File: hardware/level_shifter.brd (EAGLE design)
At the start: 15.2 x 12.7 mm, 14 parts, among them Q1 BS170, Q2 BS170

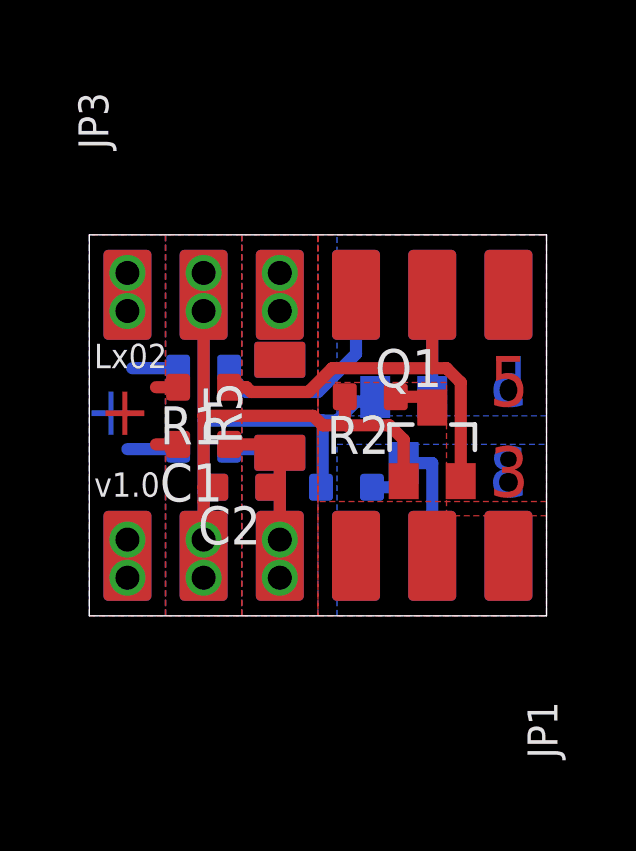
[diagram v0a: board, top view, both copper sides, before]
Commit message: shrunk level_shifter by one signal pinhead
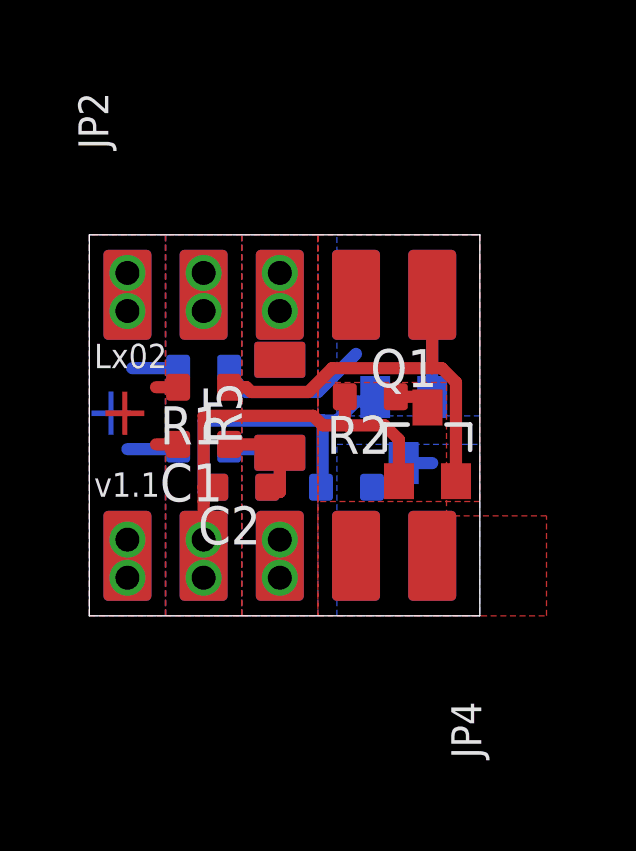
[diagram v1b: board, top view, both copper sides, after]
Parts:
- removed JP1, JP3: PINH2X06, pinhead_smd:PINH2X06SMD
- added JP2, JP4: PINH2X05, pinhead_smd:PINH2X05SMD
- moved Q1 0.16 mm to (11.3, 5.71)
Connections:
- net +3V3: now also JP2.B2, JP2.T2, JP4.B4, JP4.T4; no longer JP1.B5, JP1.T5, JP3.B2, JP3.T2
- net +5V: now also JP2.B1, JP2.T1, JP4.B5, JP4.T5; no longer JP1.B6, JP1.T6, JP3.B1, JP3.T1
- net GND: now also JP2.B3, JP2.T3, JP4.B3, JP4.T3; no longer JP1.B4, JP1.T4, JP3.B3, JP3.T3
- net IN_B: now also JP4.B1, JP4.B2; no longer JP1.B1, JP1.B2, JP1.B3
- net IN_T: now also JP4.T1, JP4.T2; no longer JP1.T1, JP1.T2, JP1.T3
- net OUT_B: now also JP2.B4, JP2.B5; no longer JP3.B4, JP3.B5, JP3.B6
- net OUT_T: now also JP2.T4, JP2.T5; no longer JP3.T4, JP3.T5, JP3.T6
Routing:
- net +3V3: track 36.0 -> 24.9 mm
- net GND: track 11.6 -> 7.30 mm
- net IN_B: track 5.90 -> 2.81 mm
- net OUT_B: track 10.6 -> 8.62 mm
- net +5V: track 5.24 -> 4.70 mm
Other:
- board size 15.2 x 12.7 mm -> 13 x 12.7 mm
- board text added: "v1.1"
- board text removed: "5"
- board text removed: "v1.0"

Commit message: level_shifter: repair one polygon and add license to schema
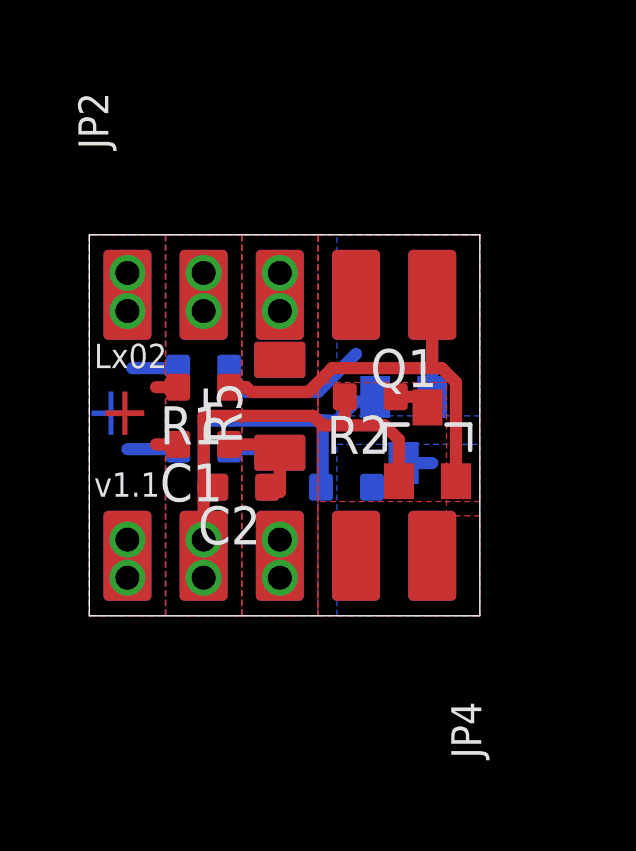
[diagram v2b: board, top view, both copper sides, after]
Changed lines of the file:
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@@
 <?xml version="1.0" encoding="utf-8"?>
 <!DOCTYPE eagle SYSTEM "eagle.dtd">
-<eagle version="7.2.0">
+<eagle version="8.1.1">
 <drawing>
 <settings>
@@
 <layer number="48" name="Document" color="7" fill="1" visible="yes" active="yes"/>
 <layer number="49" name="Reference" color="7" fill="1" visible="yes" active="yes"/>
+<layer number="50" name="dxf" color="7" fill="1" visible="no" active="no"/>
 <layer number="51" name="tDocu" color="7" fill="1" visible="yes" active="yes"/>
 <layer number="52" name="bDocu" color="7" fill="1" visible="yes" active="yes"/>
+<layer number="53" name="tGND_GNDA" color="7" fill="9" visible="no" active="no"/>
+<layer number="54" name="bGND_GNDA" color="1" fill="9" visible="no" active="no"/>
+<layer number="55" name="tPotisk" color="7" fill="1" visible="no" active="no"/>
+<layer number="56" name="wert" color="7" fill="1" visible="no" active="no"/>
+<layer number="57" name="tCAD" color="7" fill="1" visible="no" active="no"/>
+<layer number="58" name="bNC" color="7" fill="1" visible="no" active="no"/>
+<layer number="59" name="tCarbon" color="7" fill="1" visible="no" active="no"/>
+<layer number="60" name="bCarbon" color="7" fill="1" visible="no" active="no"/>
+<layer number="61" name="stand" color="7" fill="1" visible="no" active="no"/>
 <layer number="90" name="Modules" color="5" fill="1" visible="no" active="no"/>
 <layer number="91" name="Nets" color="2" fill="1" visible="no" active="no"/>
@@
 <layer number="97" name="Info" color="7" fill="1" visible="no" active="no"/>
 <layer number="98" name="Guide" color="6" fill="1" visible="no" active="no"/>
+<layer number="99" name="SpiceOrder" color="7" fill="1" visible="no" active="no"/>
 <layer number="100" name="tPlaceOutOfBoard" color="7" fill="1" visible="yes" active="yes"/>
 <layer number="101" name="bPlaceOutOfBoard" color="7" fill="1" visible="yes" active="yes"/>
+<layer number="102" name="Vscore" color="7" fill="1" visible="yes" active="yes"/>
+<layer number="103" name="tMap" color="7" fill="1" visible="yes" active="yes"/>
+<layer number="104" name="Name" color="16" fill="1" visible="yes" active="yes"/>
+<layer number="105" name="tPlate" color="7" fill="1" visible="yes" active="yes"/>
+<layer number="106" name="bPlate" color="7" fill="1" visible="yes" active="yes"/>
+<layer number="107" name="Crop" color="7" fill="1" visible="yes" active="yes"/>
+<layer number="108" name="fp8" color="7" fill="1" visible="no" active="yes"/>
+<layer number="109" name="fp9" color="7" fill="1" visible="no" active="yes"/>
+<layer number="110" name="fp0" color="7" fill="1" visible="no" active="yes"/>
+<layer number="111" name="LPC17xx" color="7" fill="1" visible="no" active="yes"/>
+<layer number="112" name="tSilk" color="7" fill="1" visible="no" active="yes"/>
+<layer number="113" name="ReferenceLS" color="7" fill="1" visible="no" active="no"/>
+<layer number="116" name="Patch_BOT" color="9" fill="4" visible="yes" active="yes"/>
+<layer number="118" name="Rect_Pads" color="7" fill="1" visible="no" active="no"/>
+<layer number="121" name="_tsilk" color="7" fill="1" visible="yes" active="yes"/>
+<layer number="122" name="_bsilk" color="7" fill="1" visible="yes" active="yes"/>
+<layer number="123" name="tTestmark" color="7" fill="1" visible="no" active="yes"/>
+<layer number="124" name="bTestmark" color="7" fill="1" visible="no" active="yes"/>
+<layer number="125" name="_tNames" color="7" fill="1" visible="no" active="yes"/>
+<layer number="126" name="_bNames" color="7" fill="1" visible="no" active="yes"/>
+<layer number="127" name="_tValues" color="7" fill="1" visible="no" active="yes"/>
+<layer number="128" name="_bValues" color="7" fill="1" visible="no" active="yes"/>
+<layer number="129" name="Mask" color="7" fill="1" visible="yes" active="yes"/>
+<layer number="131" name="tAdjust" color="7" fill="1" visible="no" active="yes"/>
+<layer number="132" name="bAdjust" color="7" fill="1" visible="no" active="yes"/>
+<layer number="144" name="Drill_legend" color="7" fill="1" visible="yes" active="yes"/>
+<layer number="150" name="Notes" color="7" fill="1" visible="no" active="yes"/>
+<layer number="151" name="HeatSink" color="7" fill="1" visible="yes" active="yes"/>
+<layer number="152" name="_bDocu" color="7" fill="1" visible="no" active="yes"/>
+<layer number="153" name="FabDoc1" color="6" fill="1" visible="no" active="no"/>
+<layer number="154" name="FabDoc2" color="2" fill="1" visible="no" active="no"/>
+<layer number="155" name="FabDoc3" color="7" fill="15" visible="no" active="no"/>
+<layer number="199" name="Contour" color="7" fill="1" visible="no" active="yes"/>
+<layer number="200" name="200bmp" color="1" fill="10" visible="yes" active="yes"/>
+<layer number="201" name="201bmp" color="2" fill="1" visible="no" active="no"/>
+<layer number="202" name="202bmp" color="3" fill="1" visible="no" active="no"/>
+<layer number="203" name="203bmp" color="4" fill="10" visible="yes" active="yes"/>
+<layer number="204" name="204bmp" color="5" fill="10" visible="yes" active="yes"/>
+<layer number="205" name="205bmp" color="6" fill="10" visible="yes" active="yes"/>
+<layer number="206" name="206bmp" color="7" fill="10" visible="yes" active="yes"/>
+<layer number="207" name="207bmp" color="8" fill="10" visible="yes" active="yes"/>
+<layer number="208" name="208bmp" color="9" fill="10" visible="yes" active="yes"/>
+<layer number="209" name="209bmp" color="7" fill="1" visible="yes" active="yes"/>
+<layer number="210" name="210bmp" color="7" fill="1" visible="yes" active="yes"/>
+<layer number="211" name="211bmp" color="7" fill="1" visible="yes" active="yes"/>
+<layer number="212" name="212bmp" color="7" fill="1" visible="yes" active="yes"/>
+<layer number="213" name="213bmp" color="7" fill="1" visible="yes" active="yes"/>
+<layer number="214" name="214bmp" color="7" fill="1" visible="yes" active="yes"/>
+<layer number="215" name="215bmp" color="7" fill="1" visible="yes" active="yes"/>
+<layer number="216" name="216bmp" color="7" fill="1" visible="yes" active="yes"/>
+<layer number="217" name="217bmp" color="18" fill="1" visible="no" active="no"/>
+<layer number="218" name="218bmp" color="19" fill="1" visible="no" active="no"/>
+<layer number="219" name="219bmp" color="20" fill="1" visible="no" active="no"/>
+<layer number="220" name="220bmp" color="21" fill="1" visible="no" active="no"/>
+<layer number="221" name="221bmp" color="22" fill="1" visible="no" active="no"/>
+<layer number="222" name="222bmp" color="23" fill="1" visible="no" active="no"/>
+<layer number="223" name="223bmp" color="24" fill="1" visible="no" active="no"/>
+<layer number="224" name="224bmp" color="25" fill="1" visible="no" active="no"/>
+<layer number="225" name="225bmp" color="7" fill="1" visible="yes" active="yes"/>
+<layer number="226" name="226bmp" color="7" fill="1" visible="yes" active="yes"/>
+<layer number="227" name="227bmp" color="7" fill="1" visible="yes" active="yes"/>
+<layer number="228" name="228bmp" color="7" fill="1" visible="yes" active="yes"/>
+<layer number="229" name="229bmp" color="7" fill="1" visible="yes" active="yes"/>
+<layer number="230" name="230bmp" color="7" fill="1" visible="yes" active="yes"/>
+<layer number="231" name="Eagle3D_PG1" color="7" fill="1" visible="no" active="no"/>
+<layer number="232" name="Eagle3D_PG2" color="7" fill="1" visible="no" active="no"/>
+<layer number="233" name="Eagle3D_PG3" color="7" fill="1" visible="no" active="no"/>
+<layer number="248" name="Housing" color="7" fill="1" visible="no" active="yes"/>
+<layer number="249" name="Edge" color="7" fill="1" visible="no" active="yes"/>
+<layer number="250" name="Descript" color="7" fill="1" visible="no" active="no"/>
+<layer number="251" name="SMDround" color="7" fill="1" visible="no" active="no"/>
+<layer number="254" name="cooling" color="7" fill="1" visible="yes" active="yes"/>
+<layer number="255" name="routoute" color="7" fill="1" visible="yes" active="yes"/>
 </layers>
 <board>
@@
 <polygon width="0.4064" layer="1" isolate="0.2" rank="3">
 <vertex x="7.62" y="0"/>
-<vertex x="15.24" y="0"/>
-<vertex x="15.24" y="3.33375"/>
+<vertex x="13.0175" y="0"/>
+<vertex x="13.0175" y="3.33375"/>
 <vertex x="11.90625" y="3.33375"/>
 <vertex x="11.90625" y="7.77875"/>
